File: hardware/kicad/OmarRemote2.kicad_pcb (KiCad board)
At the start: 2 copper layers, 27 parts, among them J1 USB_C_Receptacle_USB2.0_16P, J2 Conn_01x03, SW1 SW_Push, SW2 SW_Push, SW3 SW_Push, SW4 SW_Push, SW5 SW_Push, SW6 SW_Push, SW7 SW_DIP_x01, U1 XIAO-ESP32-S3-SMD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

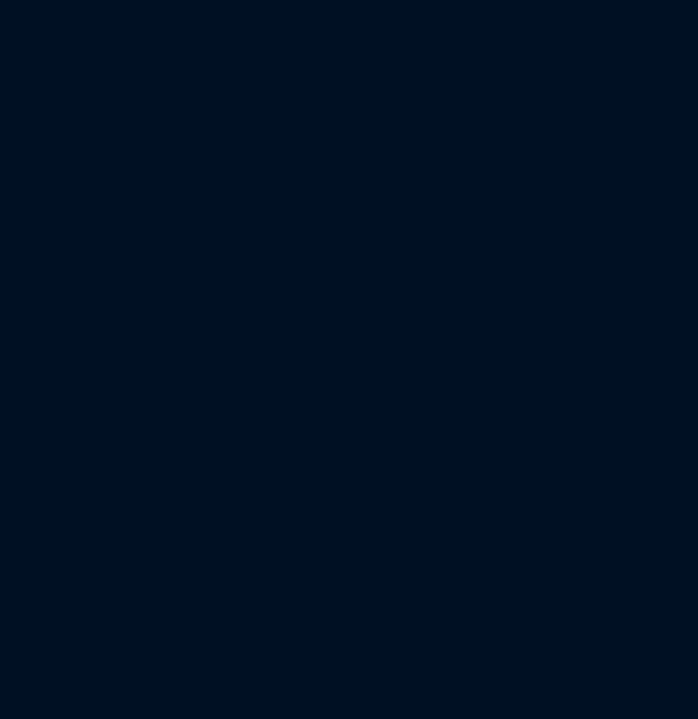
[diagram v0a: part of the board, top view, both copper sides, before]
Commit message: update sch to exclude IR
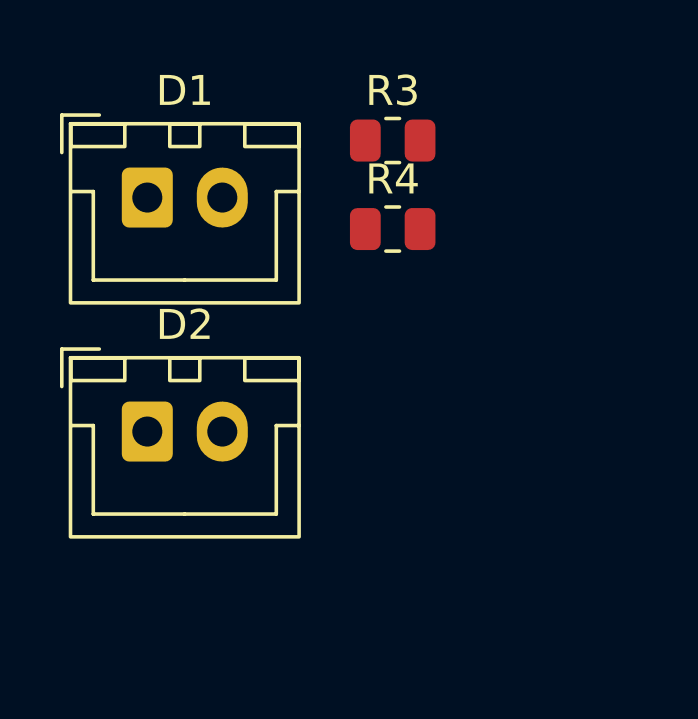
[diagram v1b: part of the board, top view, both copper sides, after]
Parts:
- added D1: LED, Connector_JST:JST_XH_B2B-XH-A_1x02_P2.50mm_Vertical, F.Cu at (2.98, 2.88)
- added D2: LED, Connector_JST:JST_XH_B2B-XH-A_1x02_P2.50mm_Vertical, F.Cu at (2.98, 10.7)
- added R3: R, Resistor_SMD:R_0805_2012Metric, F.Cu at (11.2, 0.97)
- added R4: R, Resistor_SMD:R_0805_2012Metric, F.Cu at (11.2, 3.92)
- SW1: value SW_Push -> ButtonOK
- SW2: value SW_Push -> ButtonBACK
- SW3: value SW_Push -> ButtonUP
- SW4: value SW_Push -> ButtonDOWN
- SW5: value SW_Push -> ButtonRIGHT
- SW6: value SW_Push -> ButtonLEFT
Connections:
- net ButtonBACK renamed ButtonBACK-Pin
- net ButtonDOWN renamed ButtonDOWN-PIN
- net ButtonLEFT renamed ButtonLEFT-PIN
- net ButtonOK renamed ButtonOK-Pin
- net ButtonRIGHT renamed ButtonRIGHT-PIN
- net ButtonUP renamed ButtonUP-PIN
- net VoltBattery renamed BatteryVoltMeasPin
- U1 pad 7: IR -> unconnected-(U1-GPIO16_D6_TX-Pad7)
- U1 pad 8: LEDPower -> LEDPower-Pin
- U1 pad 9: LEDCharge -> LEDCharge-Pin
